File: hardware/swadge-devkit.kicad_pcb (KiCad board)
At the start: 2 copper layers, 100 x 100 mm, 56 parts, among them J1 USB_B_Micro, SW1 SW_SPDT, SW2 SW_Push, SW3 SW_Push, SW4 SW_Push, SW5 SW_Push, U1 ESP-12F, U2 MCP6001-OT, U3 MMA8452Q, U4 AP1117-33, U5 BUS_PCIexpress, U6 DISP_OLED_UG-2864HSWEG01

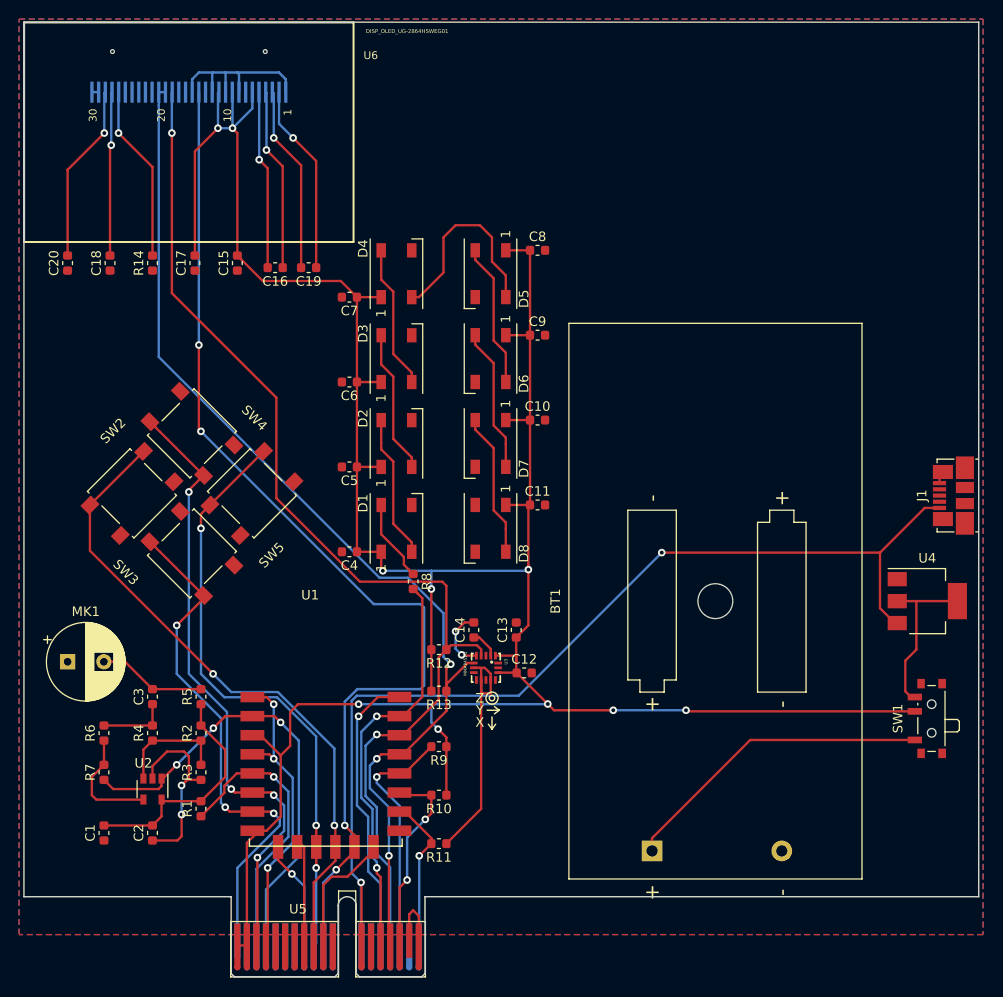
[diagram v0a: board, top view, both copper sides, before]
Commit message: Added more 3D parts!
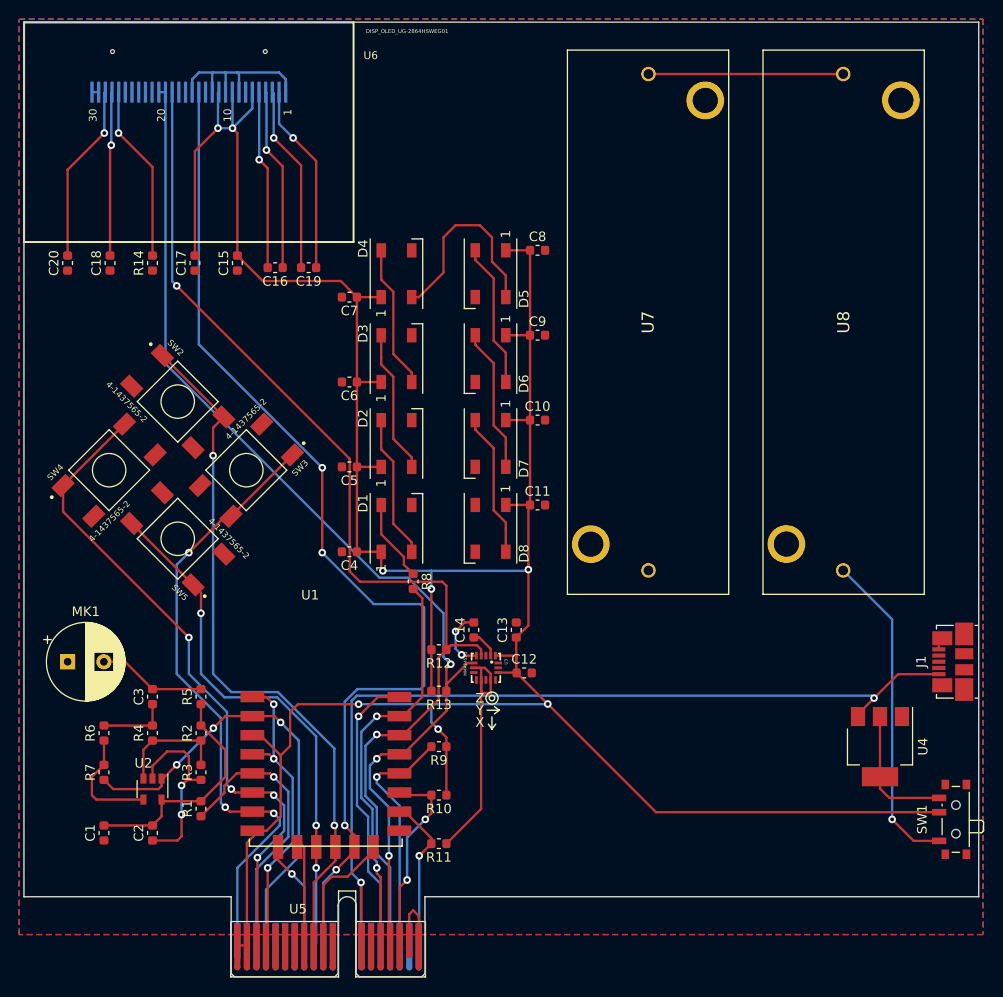
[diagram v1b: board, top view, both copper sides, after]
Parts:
- removed BT1: Battery, Battery:BatteryHolder_MPD_BC2AAPC_2xAA
- added U7: 2460, SamacSys_Parts:2460, F.Cu at (178.9, 78.7)
- added U8: 2460, SamacSys_Parts:2460, F.Cu at (199.4, 78.7)
- SW2, SW3, SW4, SW5: value SW_Push -> 4-1437565-2; footprint Button_Switch_SMD:SW_SPST_B3S-1000 -> 4-1437565-2:SW_4-1437565-2
- moved J1 17.4 mm to (210.8, 114.3)
- moved U4 16.0 mm to (203.2, 123.2), turned to 270 degrees
- moved SW1 10.9 mm to (210.8, 130.8)
- moved SW2 10.7 mm to (129.6, 87.1), turned to 315 degrees
- moved SW3 10.4 mm to (136.8, 94.2), turned to 225 degrees
- moved SW4 9.49 mm to (122.5, 94.2), turned to 45 degrees
- moved SW5 9.11 mm to (129.6, 101.4), turned to 135 degrees
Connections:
- SW2 pad 2: GND -> SW2
- SW3 pad 2: GND -> SW3
- SW4 pad 2: GND -> SW4
- SW5 pad 2: GND -> SW5
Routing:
- net Net-(U7-Pad1): track 0.00 -> 20.4 mm
- net +5V: track 110.9 -> 98.1 mm
- net SW3: track 55.0 -> 65.2 mm
- net SW5: track 62.8 -> 55.5 mm
- net +3V3: track 294.9 -> 301.3 mm, vias 10 -> 8
- net SW2: track 68.5 -> 74.0 mm
- net SW4: track 65.8 -> 70.7 mm
- net Net-(SW1-Pad3): track 17.9 -> 14.1 mm
- net Net-(SW1-Pad1): track 33.7 -> 34.1 mm, vias 0 -> 1

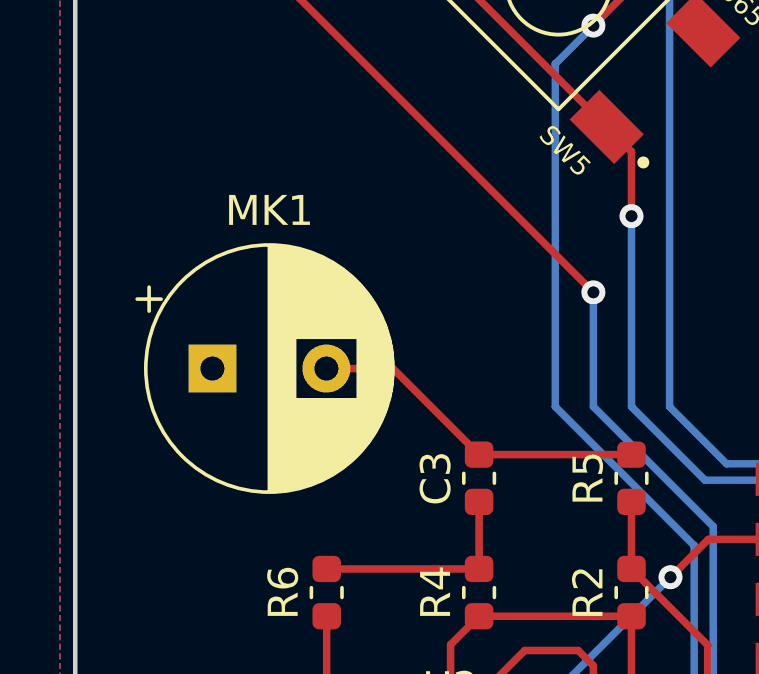
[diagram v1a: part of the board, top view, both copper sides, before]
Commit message: Made a new microphone footprint, added 3D microphone model
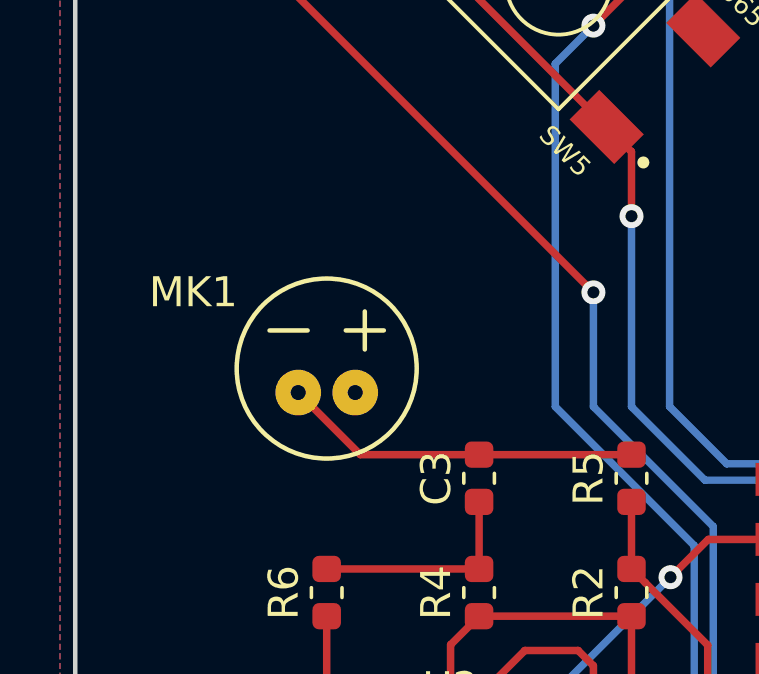
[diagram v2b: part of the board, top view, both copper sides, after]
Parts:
- MK1: footprint Capacitor_THT:CP_Radial_D8.0mm_P3.80mm -> microphone:POM-2738P-R
- moved MK1 3.81 mm to (121.9, 114.3), turned to 180 degrees
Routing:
- net Net-(C3-Pad2): track 11.4 -> 12.0 mm

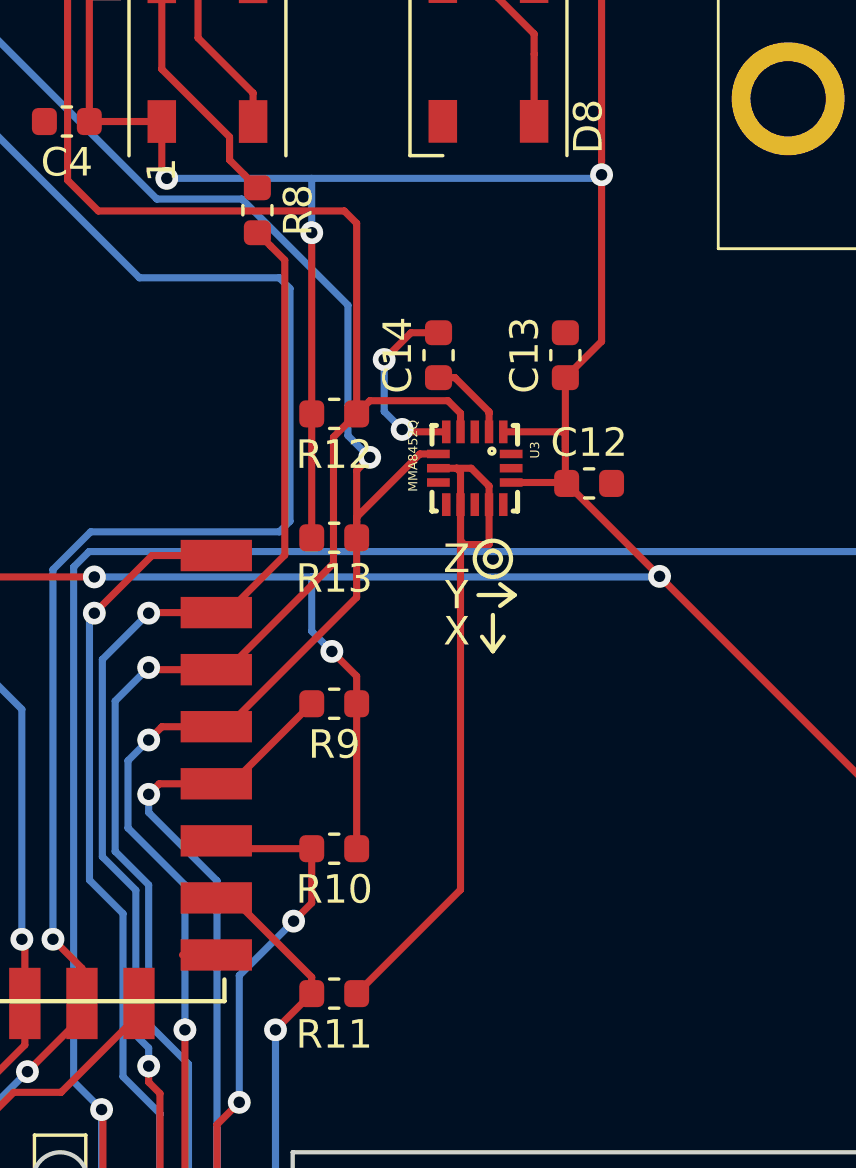
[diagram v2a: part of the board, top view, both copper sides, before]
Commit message: Replaced MMA8452Q accelerometer with MSA300
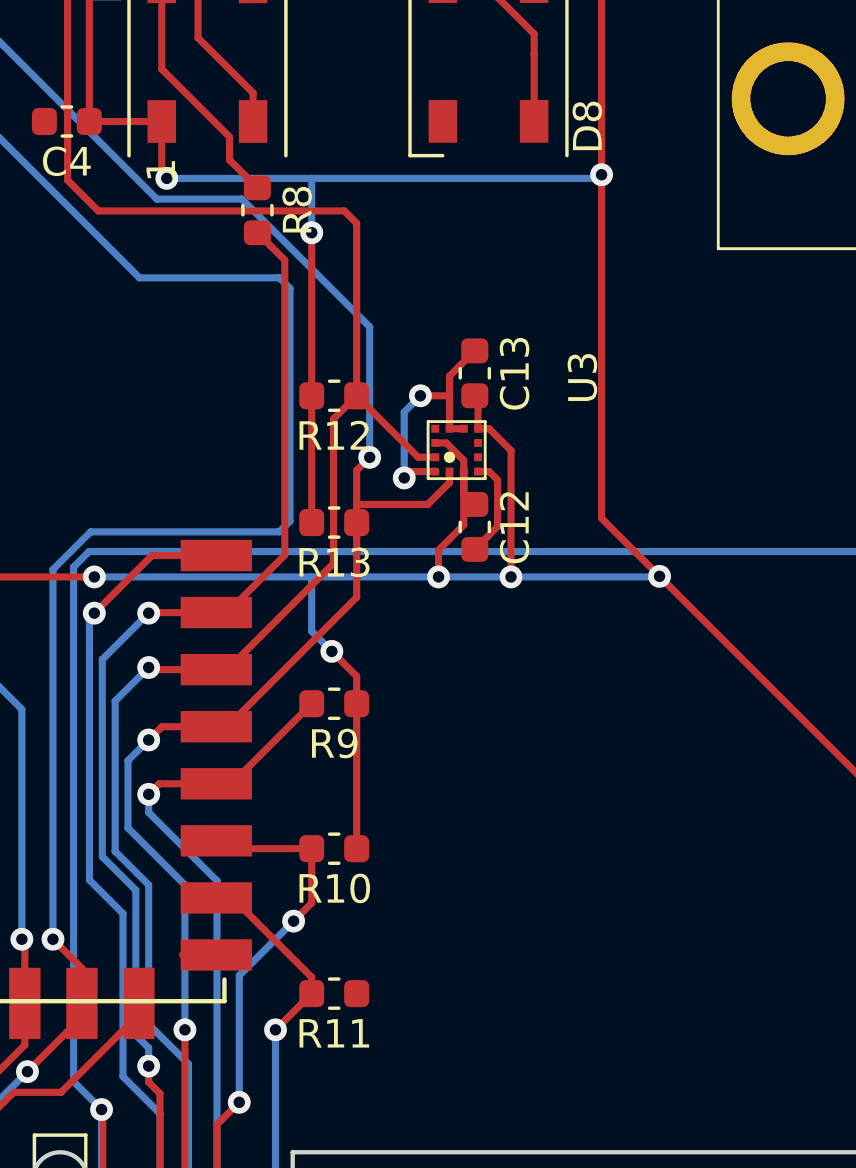
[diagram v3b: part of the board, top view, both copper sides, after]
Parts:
- removed C14: 0.1u, Capacitor_SMD:C_0603_1608Metric
- C12: value 4.7u -> 0.1u
- R12, R13: value 10k -> 4.7k
- U3: value MMA8452Q -> MSA300; footprint MMA8452Q:QFN-16_0.5MM -> MSA300:MSA300
- moved C12 4.29 mm to (161.9, 117.0), turned to 270 degrees
- moved C13 3.24 mm to (161.9, 111.6), turned to 270 degrees
- moved U3 0.90 mm to (161.3, 114.3), turned to 90 degrees
- moved R12 0.64 mm to (157.0, 112.4)
- moved R13 0.53 mm to (157.0, 116.8)
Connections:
- C13 pad 1: +3V3 -> GND
- C13 pad 2: GND -> +3V3
- U3 pad 1: +3V3 -> GND
- U3 pad 10: GND -> Net-(U3-Pad10)
- U3 pad 11: Net-(U3-Pad11) -> +3V3
- U3 pad 12: GND -> SCL
- U3 pad 2: Net-(C14-Pad1) -> SDA
- U3 pad 3: (no net) -> +3V3
- U3 pad 4: SCL -> GND
- U3 pad 5: GND -> Net-(U3-Pad5)
- U3 pad 6: SDA -> Net-(U3-Pad6)
- U3 pad 7: GND -> +3V3
- U3 pad 8: (no net) -> GND
- U3 pad 9: Net-(U3-Pad9) -> GND
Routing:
- net GND: track 82.4 -> 63.2 mm
- net +3V3: track 301.3 -> 309.1 mm, vias 8 -> 10
- net Net-(C14-Pad1): track 2.97 -> 0.00 mm
- net SCL: track 117.3 -> 116.3 mm

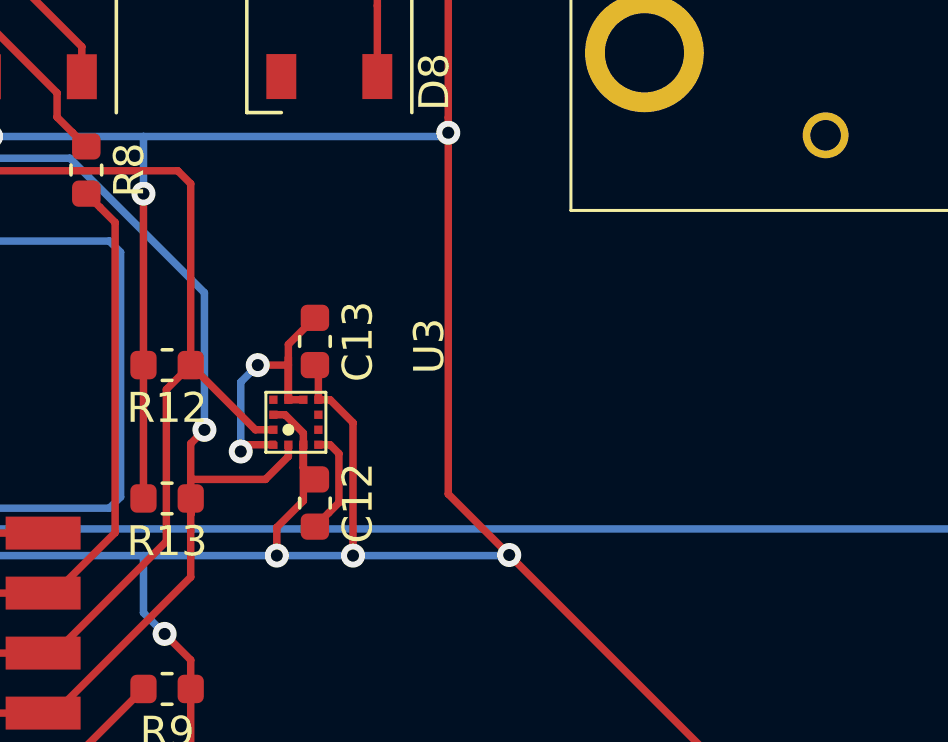
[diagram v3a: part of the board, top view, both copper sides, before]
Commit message: Added second accelerometer, MMA8452Q
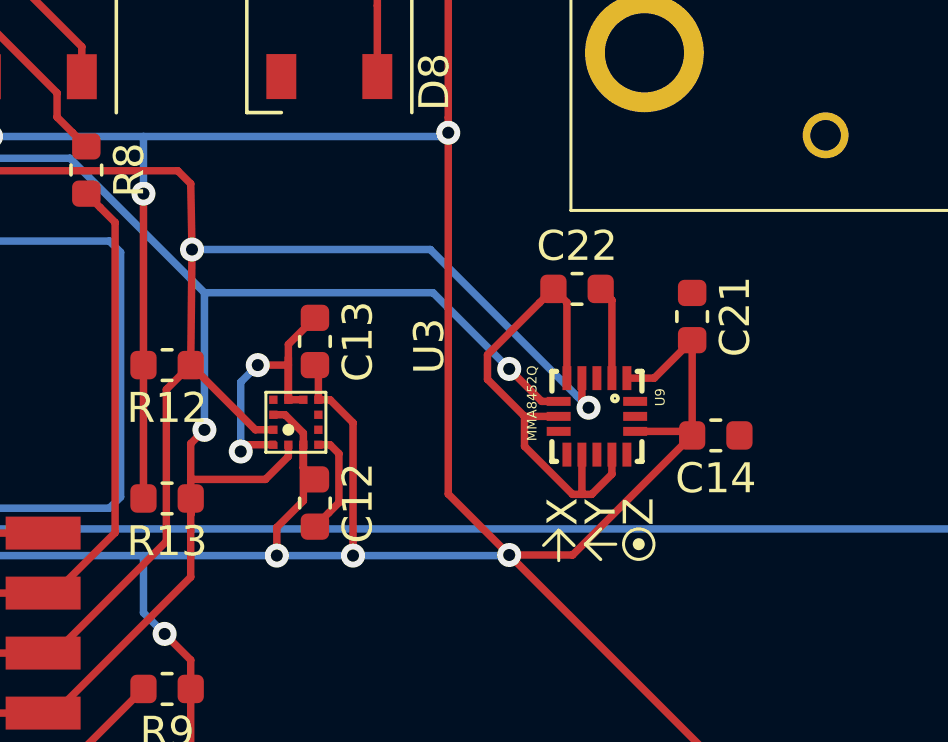
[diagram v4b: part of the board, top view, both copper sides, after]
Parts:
- added C14: 0.1u, Capacitor_SMD:C_0603_1608Metric, F.Cu at (175.3, 114.7)
- added C21: 0.1u, Capacitor_SMD:C_0603_1608Metric, F.Cu at (174.5, 110.8)
- added C22: 0.1u, Capacitor_SMD:C_0603_1608Metric, F.Cu at (170.7, 109.9)
- added U9: MMA8452Q, MMA8452Q:QFN-16_0.5MM, F.Cu at (171.3, 114.1)
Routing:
- net GND: track 63.2 -> 80.0 mm
- net SCL: track 116.3 -> 132.8 mm, vias 2 -> 4
- net +3V3: track 309.1 -> 324.6 mm
- net SDA: track 114.6 -> 127.9 mm, vias 3 -> 4
- net Net-(C22-Pad2): track 0.00 -> 3.13 mm

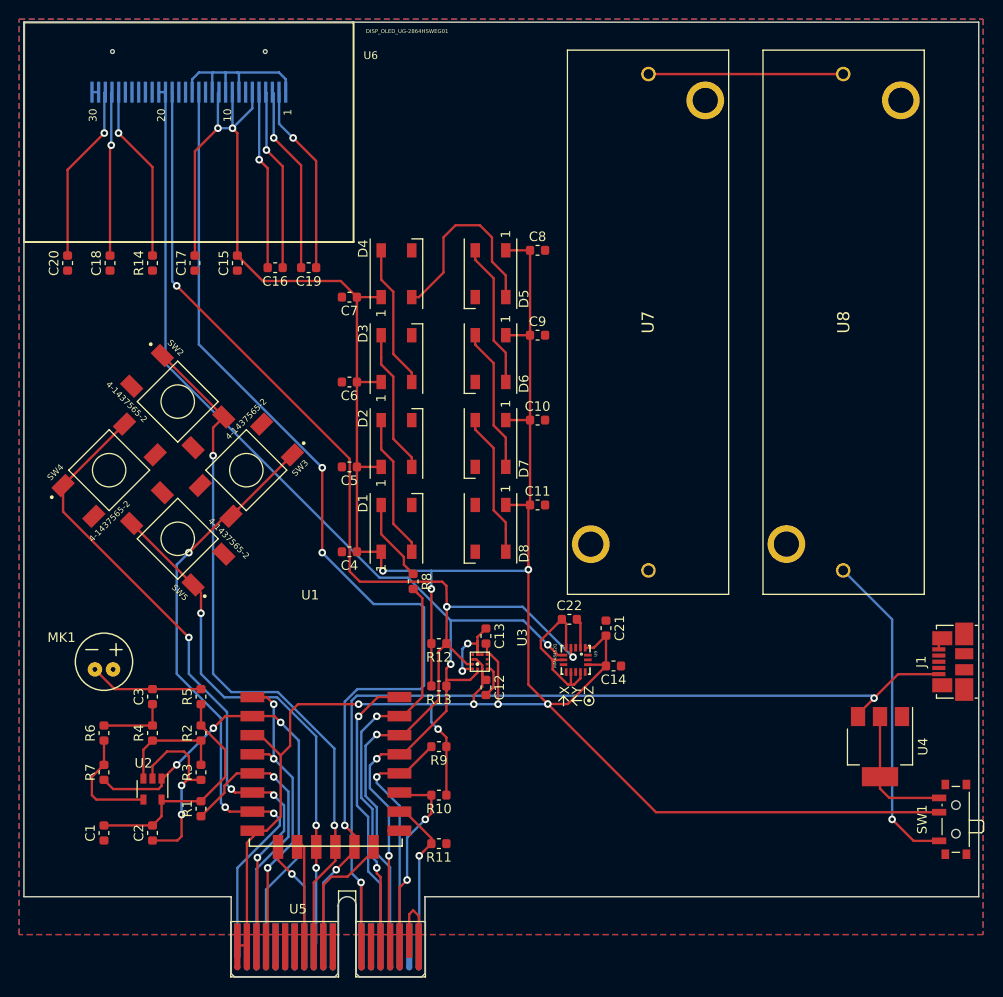
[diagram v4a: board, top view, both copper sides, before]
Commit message: Merged libraries, footprints, and 3d shapes
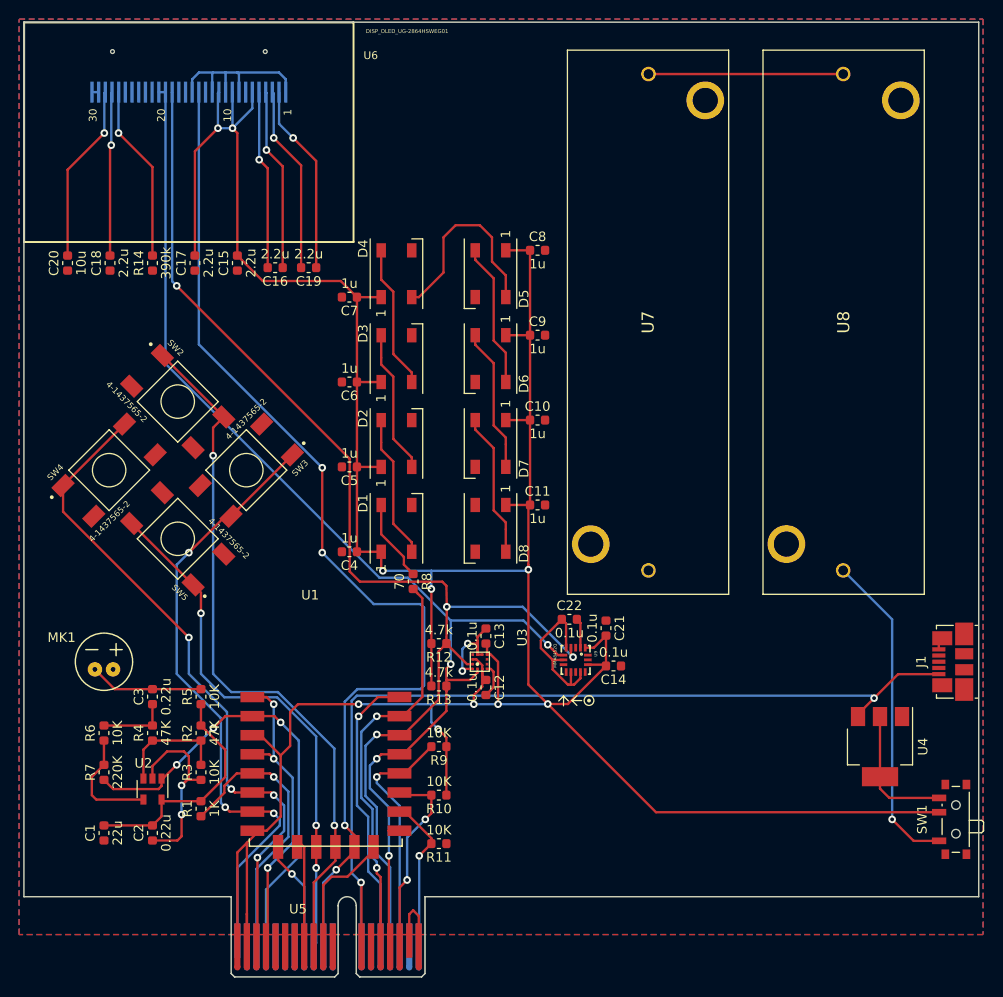
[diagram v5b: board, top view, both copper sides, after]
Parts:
- C1, C10, C11, C12, C13, C14, C15, C16, C17, C18, C19, C2, C20, C21, C22, C3, C4, C5, C6, C7, C8, C9: footprint Capacitor_SMD:C_0603_1608Metric -> Swadge_Parts:C_0603_1608Metric
- D1, D2, D3, D4, D5, D6, D7, D8: footprint LED_SMD:LED_WS2812B_PLCC4_5.0x5.0mm_P3.2mm -> Swadge_Parts:LED_WS2812B_PLCC4_5.0x5.0mm_P3.2mm
- J1: footprint Connector_USB:USB_Micro-B_Molex_47346-0001 -> Swadge_Parts:USB_Micro-B_Molex_47346-0001
- MK1: footprint microphone:POM-2738P-R -> Swadge_Parts:POM-2738P-R
- R1, R10, R11, R12, R13, R14, R2, R3, R4, R5, R6, R7, R8, R9: footprint Resistor_SMD:R_0603_1608Metric -> Swadge_Parts:R_0603_1608Metric
- SW1: footprint Button_Switch_SMD:SW_SPDT_PCM12 -> Swadge_Parts:SW_SPDT_PCM12
- SW2, SW3, SW4, SW5: footprint 4-1437565-2:SW_4-1437565-2 -> Swadge_Parts:SW_4-1437565-2
- U1: footprint ESP8266:ESP-12E_SMD -> Swadge_Parts:ESP-12E_SMD
- U2: footprint Package_TO_SOT_SMD:SOT-23-5 -> Swadge_Parts:SOT-23-5
- U3: footprint MSA300:MSA300 -> Swadge_Parts:MSA300
- U4: footprint Package_TO_SOT_SMD:SOT-223-3_TabPin2 -> Swadge_Parts:SOT-223-3_TabPin2
- U5: footprint Connector_PCBEdge:BUS_PCIexpress -> Swadge_Parts:BUS_PCIexpress
- U6: footprint disp_oled:microbuilder-UG-2864HSWEG01_1.3_WRAPAROUND -> Swadge_Parts:microbuilder-UG-2864HSWEG01_1.3_WRAPAROUND
- U7, U8: footprint SamacSys_Parts:2460 -> Swadge_Parts:2460
- U9: footprint MMA8452Q:QFN-16_0.5MM -> Swadge_Parts:QFN-16_0.5MM
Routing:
- net +3V3: track 324.6 -> 338.1 mm
